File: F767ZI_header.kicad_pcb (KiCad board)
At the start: 2 copper layers, 19 parts, among them J1 I2C1_MD, J2 CAN1, J3 CAN2, J4 UART, J5 PowerBoard, J6 EMERSW_CON, J7 Encoder1, J8 Encoder2, J9 RESET_SW, SW1 SW_Push, U1 MCP2562-E-P, U2 MCP2562-E-P

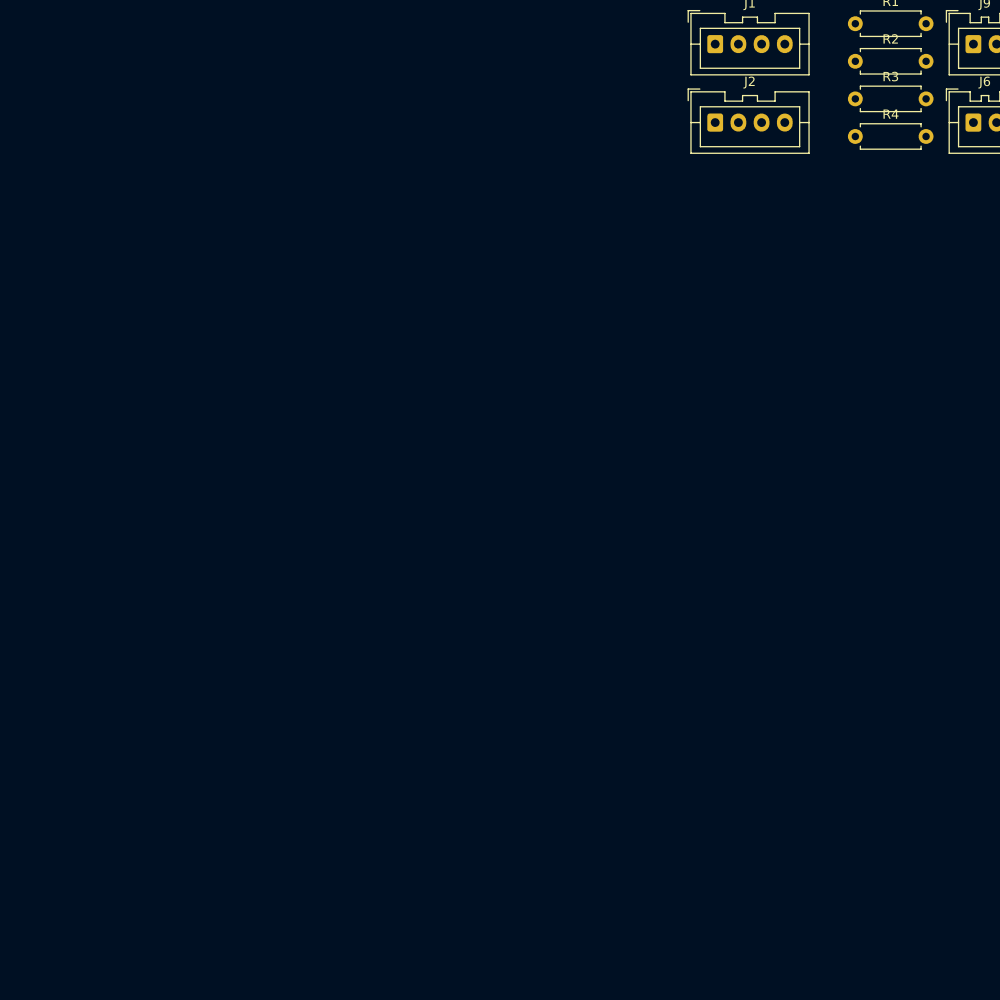
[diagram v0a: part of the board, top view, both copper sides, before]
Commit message: sch: Add a CAN connector
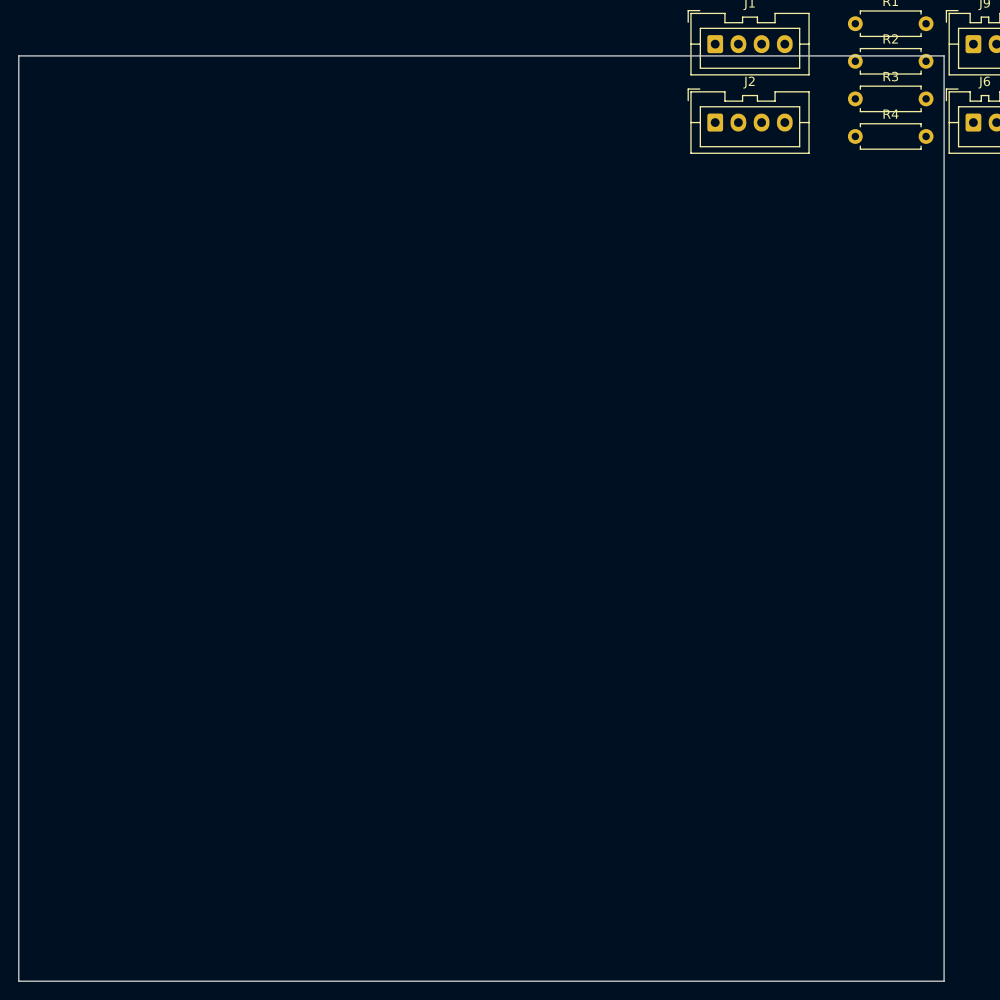
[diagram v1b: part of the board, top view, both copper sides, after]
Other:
- board outline added: 99.7 x 99.7 mm
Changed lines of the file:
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@@
 		)
 	)
+	(gr_rect
+		(start 39.37 73.66)
+		(end 139.065 173.355)
+		(stroke
+			(width 0.05)
+			(type default)
+		)
+		(fill none)
+		(layer "Edge.Cuts")
+	)
 )

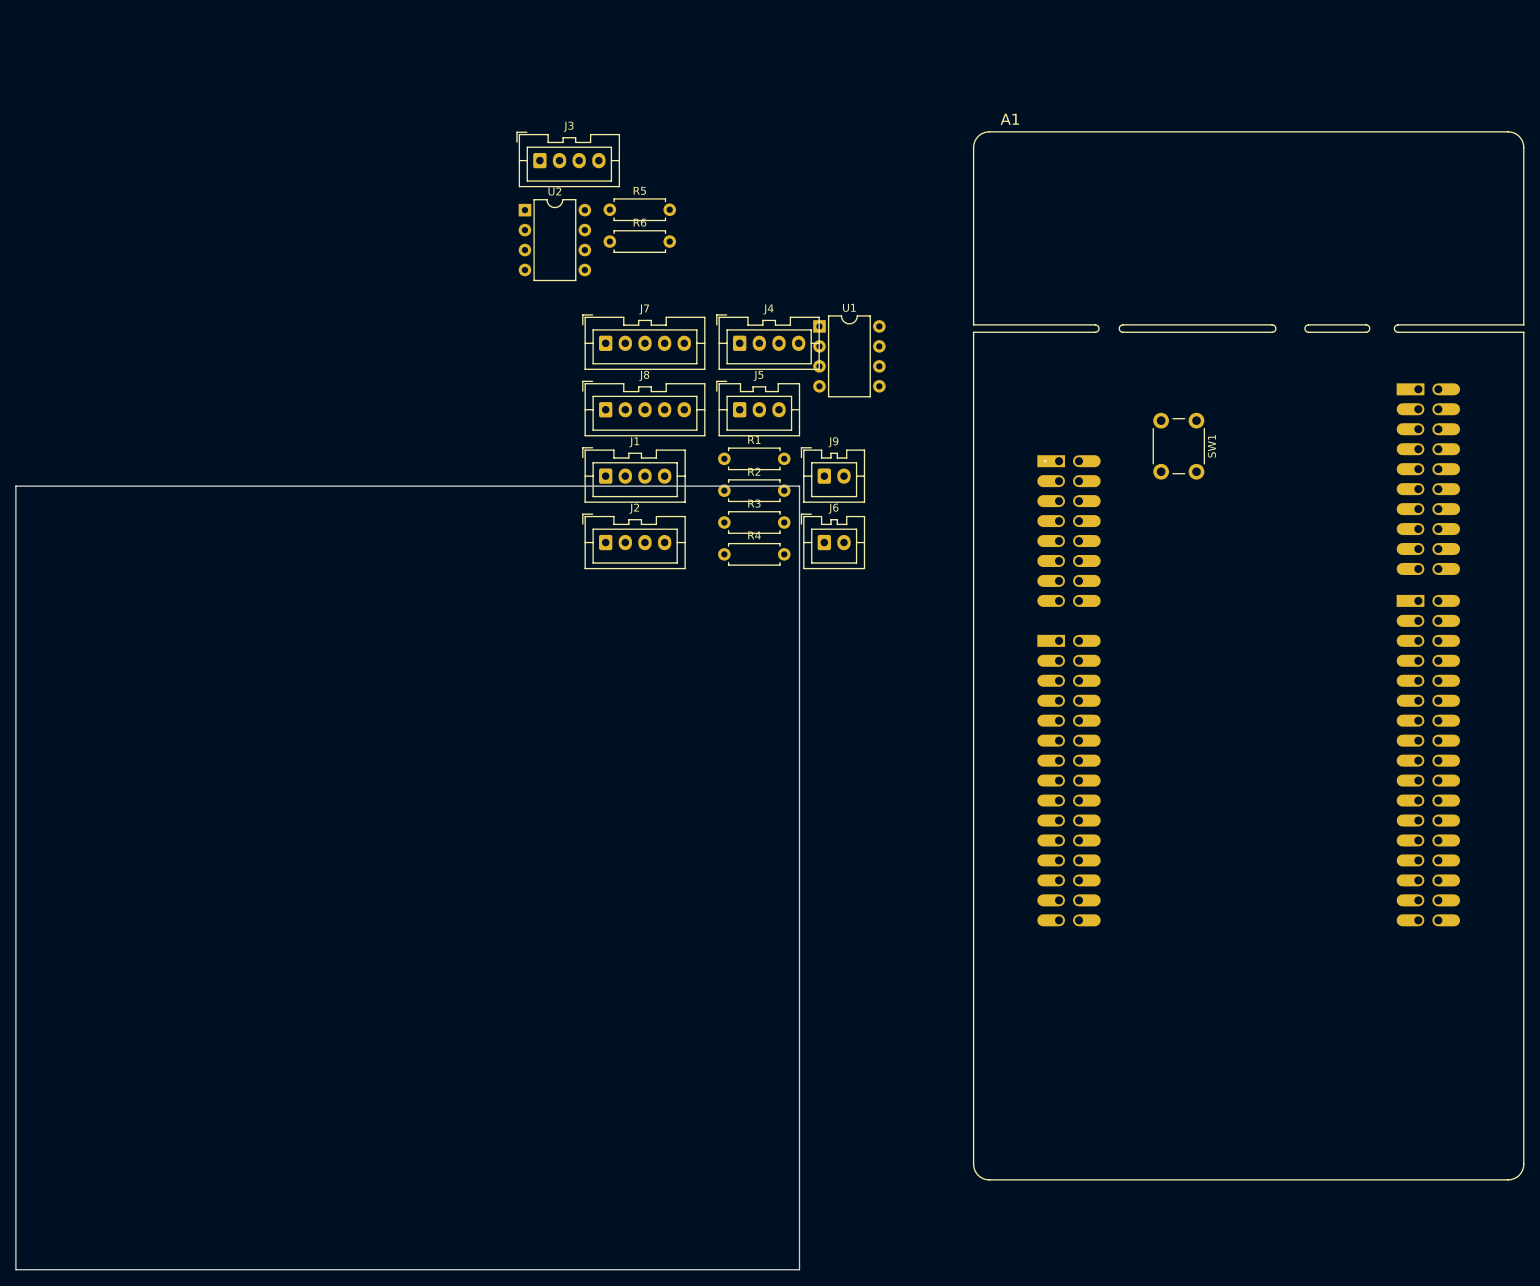
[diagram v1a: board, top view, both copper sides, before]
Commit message: PCB: Update with SCH
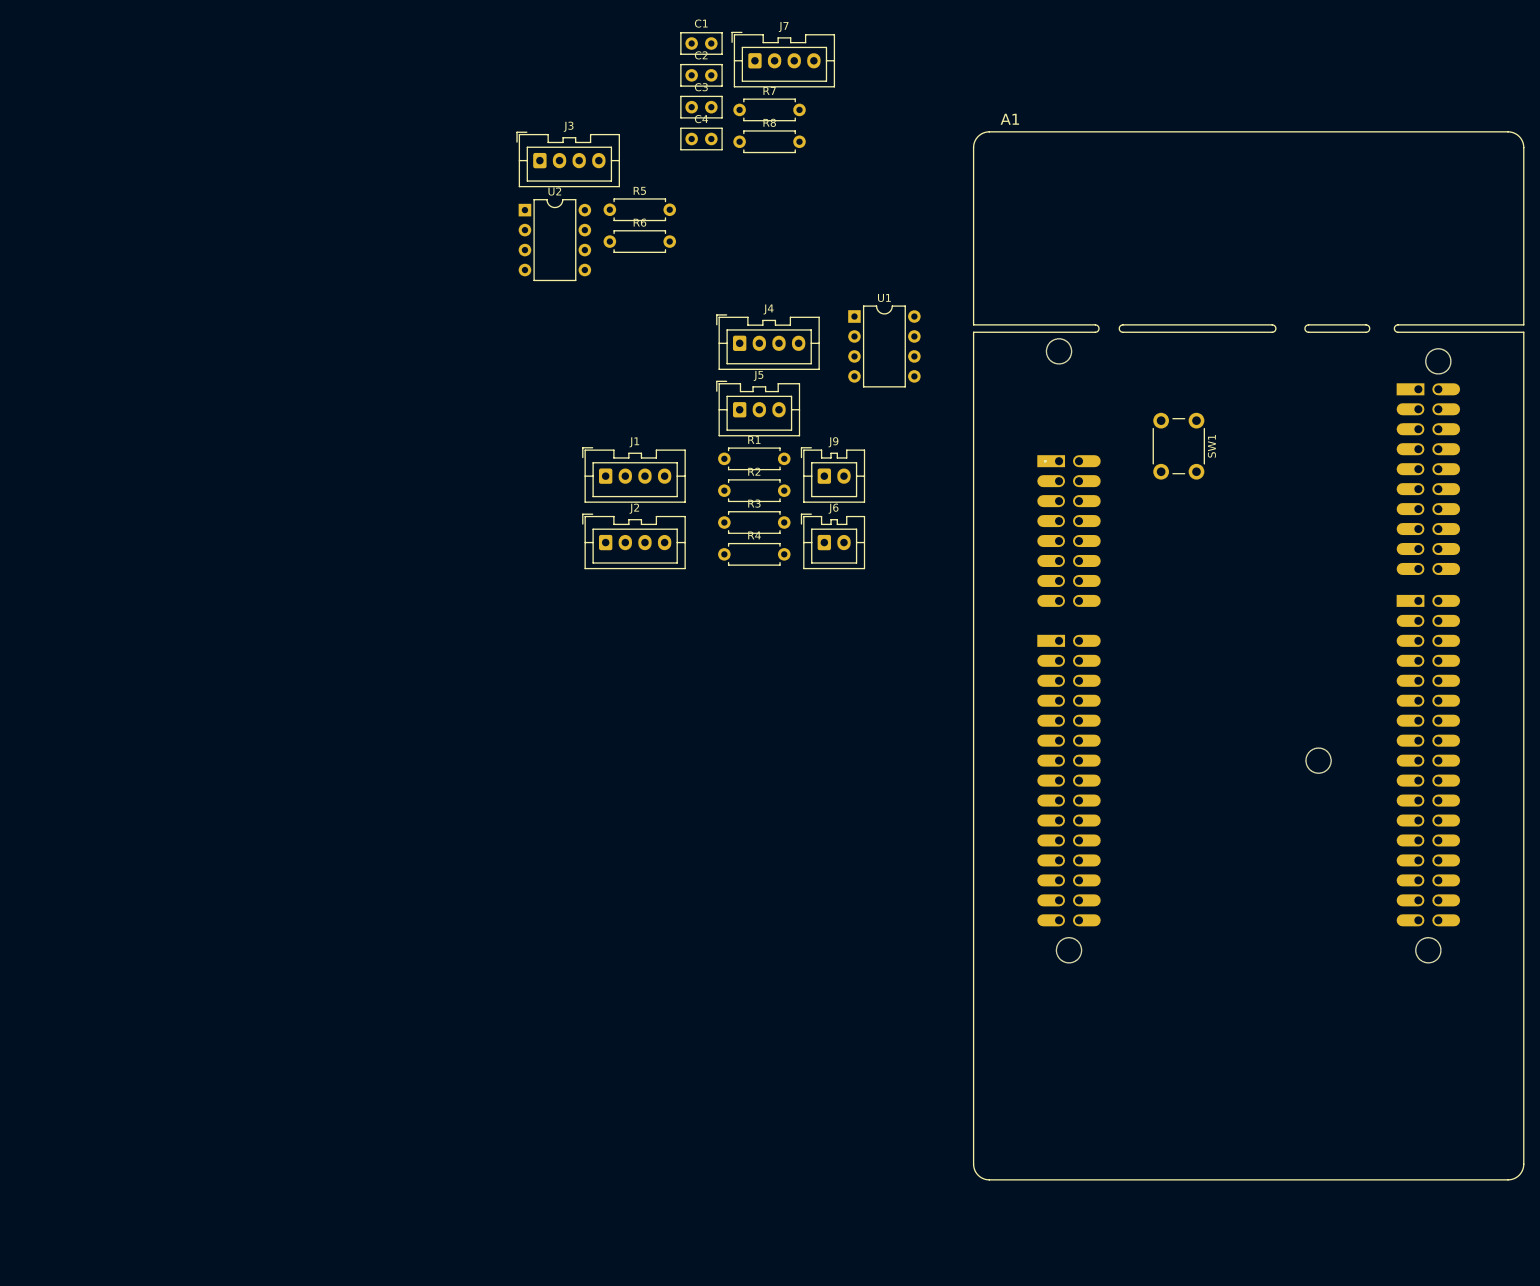
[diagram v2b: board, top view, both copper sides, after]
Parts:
- removed J8: Encoder2, Connector_JST:JST_XA_B05B-XASK-1_1x05_P2.50mm_Vertical
- added C1: 0.1u, Capacitor_THT:C_Disc_D5.0mm_W2.5mm_P2.50mm, F.Cu at (125.3, 17.3)
- added C2: 0.1u, Capacitor_THT:C_Disc_D5.0mm_W2.5mm_P2.50mm, F.Cu at (125.3, 21.4)
- added C3: 0.1u, Capacitor_THT:C_Disc_D5.0mm_W2.5mm_P2.50mm, F.Cu at (125.3, 25.4)
- added C4: 0.1u, Capacitor_THT:C_Disc_D5.0mm_W2.5mm_P2.50mm, F.Cu at (125.3, 29.5)
- added R7: 4k7, Resistor_THT:R_Axial_DIN0207_L6.3mm_D2.5mm_P7.62mm_Horizontal, F.Cu at (131.4, 25.8)
- added R8: 4k7, Resistor_THT:R_Axial_DIN0207_L6.3mm_D2.5mm_P7.62mm_Horizontal, F.Cu at (131.4, 29.8)
- J1: value I2C1_MD -> I2C2_MD
- J7: value Encoder1 -> I2C1_default; footprint Connector_JST:JST_XA_B05B-XASK-1_1x05_P2.50mm_Vertical -> Connector_JST:JST_XA_B04B-XASK-1_1x04_P2.50mm_Vertical
- moved J7 40.7 mm to (133.4, 19.5)
- moved U1 4.63 mm to (146.1, 52.1)
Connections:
- A1 pad CN7_2: unconnected-(A1A-D15/PB_8/I2C_A_SCL-PadCN7_2) -> I2C1_SCL
- A1 pad CN7_4: unconnected-(A1A-D14/PB_9/I2C_A_SDA-PadCN7_4) -> I2C1_SDA
- A1 pad CN8_1: (no net) -> unconnected-(A1B-NC-PadCN8_1)
- A1 pad CN8_2: Encoder2_A -> unconnected-(A1B-D43/PC_8/SDMMC_D0-PadCN8_2)
- A1 pad CN8_4: Encoder2_B -> unconnected-(A1B-D44/PC_9/SDMMC_D1/I2S_A_CKIN-PadCN8_4)
- A1 pad CN8_6: Encoder2_Z -> unconnected-(A1B-D45/PC_10/SDMMC_D2-PadCN8_6)
- A1 pad CN9_10: Encoder1_Z -> unconnected-(A1C-D55/PD_3/USART_B_CTS-PadCN9_10)
- A1 pad CN9_19: I2C1_SCL -> I2C2_SCL
- A1 pad CN9_21: I2C1_SDA -> I2C2_SDA
- A1 pad CN9_6: Encoder1_A -> unconnected-(A1C-D53/PD_5/USART_B_TX-PadCN9_6)
- A1 pad CN9_8: Encoder1_B -> unconnected-(A1C-D54/PD_4/USART_B_RTS-PadCN9_8)
- J1 pad 2: I2C1_SCL -> I2C2_SCL
- J1 pad 3: I2C1_SDA -> I2C2_SDA
- J2 pad 4: GND -> Net-(J2-Pin_4)
- J3 pad 4: GND -> Net-(J2-Pin_4)
- J4 pad 4: GND -> Net-(J2-Pin_4)
- J7 pad 1: Encoder1_A -> I2C1_SCL
- J7 pad 2: Encoder1_B -> I2C1_SDA
- J7 pad 3: Encoder1_Z -> +5V
- J7 pad 4: +5V -> Net-(J2-Pin_4)
- R1 pad 1: +3V3 -> NRST
- R1 pad 2: NRST -> +3V3
- R2 pad 2: I2C1_SDA -> I2C2_SDA
- R3 pad 2: I2C1_SCL -> I2C2_SCL
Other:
- board outline removed
